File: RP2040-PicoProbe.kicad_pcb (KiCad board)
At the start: 4 copper layers, 39.4 x 17.8 mm, 47 parts, among them J1 CONN_MCU_DEBUG, J2 CONN_DBG_COMB, J5 USB_B_Micro, J7 CONN_DBG_JTAG, U1 W25Q128JVS, U2 RP2040, U3 74AUP1T17, U4 W25Q128JVEIQ, U5 MIC5205-3.3YM5, U6 74AUP1T17, Y1 12MHz

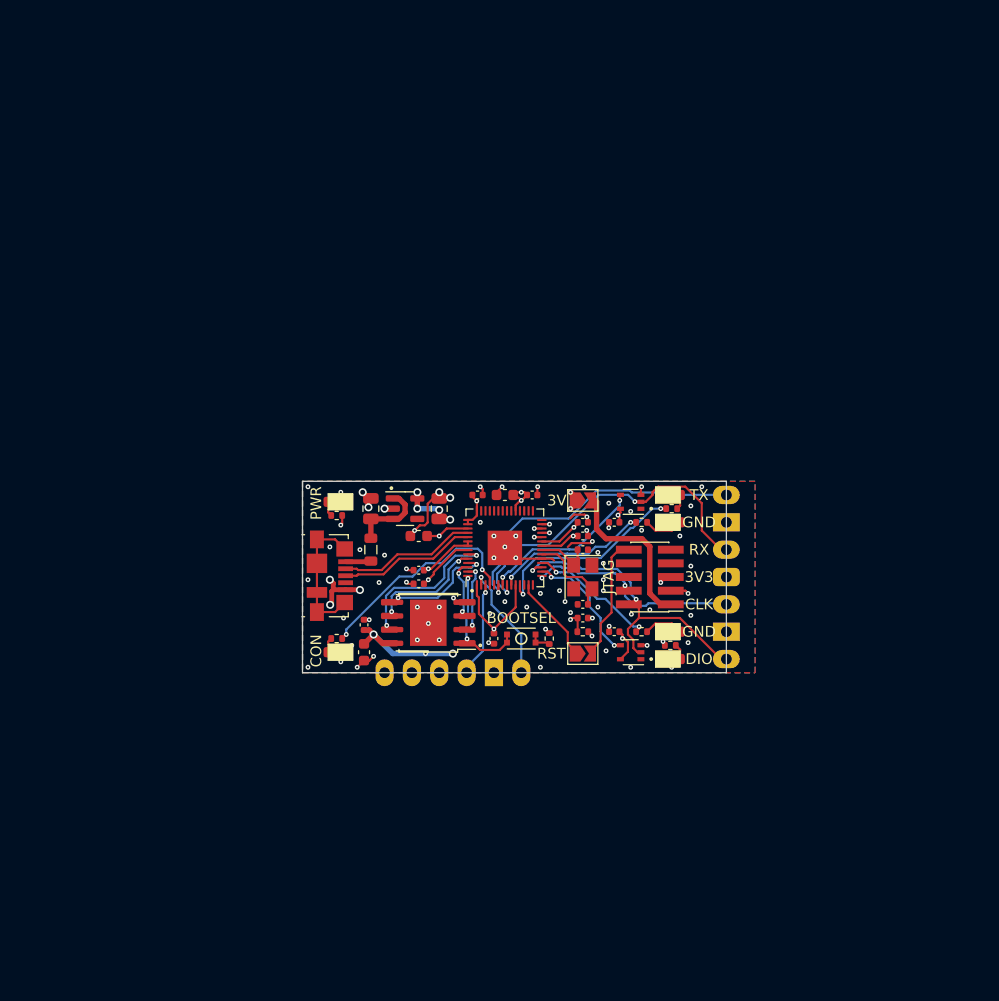
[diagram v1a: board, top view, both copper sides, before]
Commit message: Removed host debug part. Moved secondary components to the back of the board.
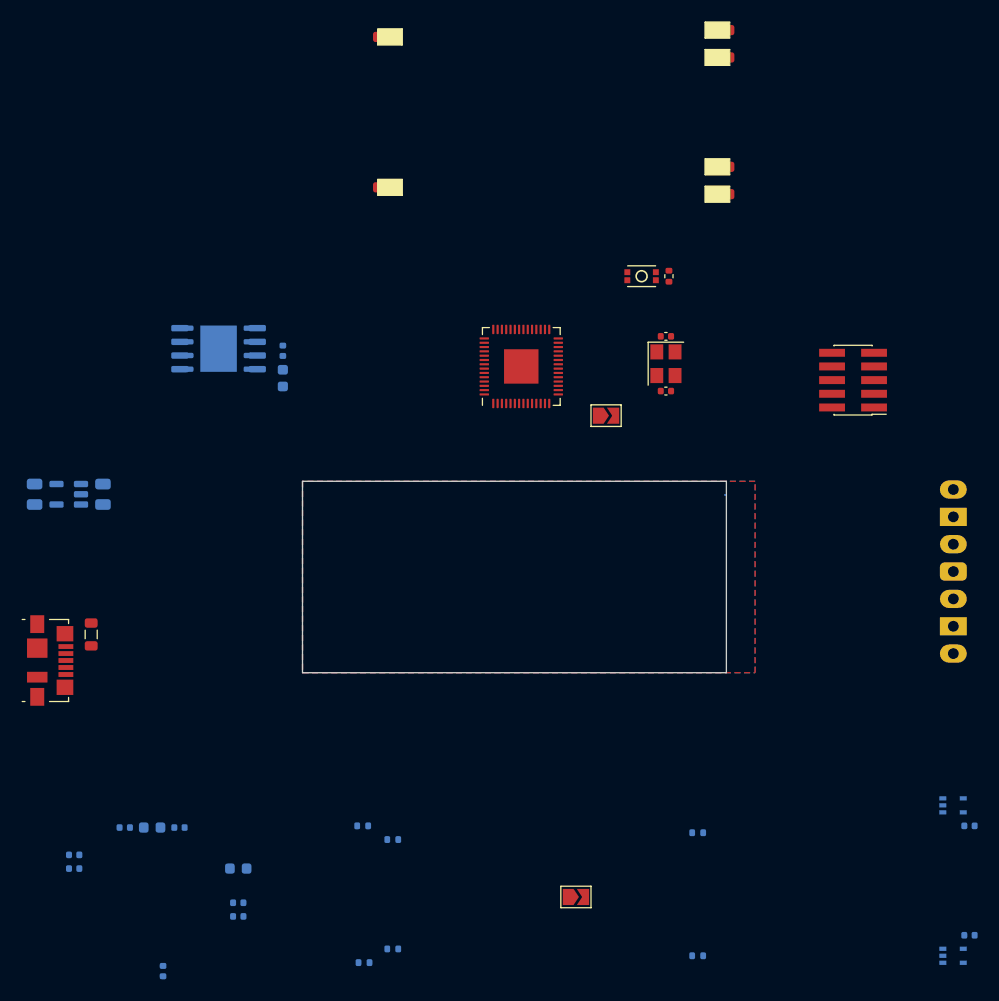
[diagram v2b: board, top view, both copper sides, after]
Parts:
- removed C12: 100nF, Capacitor_SMD:C_0402_1005Metric
- removed J1: CONN_MCU_DEBUG, Connector_PinHeader_2.54mm:PinHeader_1x06_P2.54mm_Vertical
- removed R8: 10k, Resistor_SMD:R_0402_1005Metric
- C1, C10, C11, C13, C14, C15, C16, C17, C18, C2, C4, C5, C6, C8, C9, R1, R2, R3, R4, R5, R6, U1, U3, U4, U5, U6: moved to B.Cu
- moved C11 56.4 mm to (105.8, 128.4), turned to 180 degrees
- moved C18 56.4 mm to (105.8, 127.2), turned to 180 degrees
- moved C4 48.9 mm to (110.5, 124.6), turned to 180 degrees
- moved C1 45.0 mm to (113.0, 124.6), turned to 0 degrees
- moved R3 44.6 mm to (163.7, 136.5), turned to 0 degrees
- moved R6 44.6 mm to (163.7, 125.1), turned to 0 degrees
- moved C10 43.6 mm to (114.0, 137.9)
- moved D1 43.4 mm to (165.9, 53.1)
- moved D2 43.4 mm to (134.8, 51.2)
- moved D5 43.4 mm to (134.8, 65.2)
- moved D4 43.4 mm to (165.9, 50.5)
- moved D6 43.4 mm to (165.9, 63.2)
- moved D7 43.4 mm to (165.9, 65.8)
- moved C13 43.4 mm to (188.9, 134.6), turned to 0 degrees
- moved C17 43.4 mm to (188.9, 124.5), turned to 0 degrees
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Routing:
- net +3V3: track 52.5 -> 0.00 mm, vias 19 -> 0
- net GND: track 43.4 -> 0.00 mm, vias 83 -> 0
- net TARGET_RX: track 32.4 -> 0.00 mm, vias 2 -> 0
- net +1V1: track 32.0 -> 0.00 mm, vias 3 -> 0
- net DBG_DIO: track 29.7 -> 0.00 mm, vias 2 -> 0
- net TARGET_TX: track 29.4 -> 0.02 mm, vias 1 -> 0
- net HOST_RESET: track 28.5 -> 0.00 mm, vias 2 -> 0
- net HOST_DIO: track 25.4 -> 0.00 mm, vias 1 -> 0
- net HOST_CLK: track 23.1 -> 0.00 mm, vias 1 -> 0
- net DBG_CLK: track 20.8 -> 0.00 mm, vias 2 -> 0
- net LED_ACT: track 20.1 -> 0.00 mm, vias 2 -> 0
- net LED_TX: track 18.8 -> 0.00 mm, vias 2 -> 0
- net LED_RUN: track 17.3 -> 0.00 mm, vias 2 -> 0
- net TARGET_3V3: track 15.5 -> 0.00 mm
- net UART_RX_BUF: track 15.4 -> 0.00 mm, vias 2 -> 0
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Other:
- board text removed: "${TITLE} ${COMPANY} ${COMMENT2}"
- board text removed: "3V"
- board text removed: "3V3"
- board text removed: "BOOTSEL"
- board text removed: "CLK"
- board text removed: "CON"
- board text removed: "DIO"
- board text removed: "GND"
- board text removed: "JTAG"
- board text removed: "PWR"
- board text removed: "RST"
- board text removed: "RX"
- board text removed: "TX"

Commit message: Roughly put components to their places
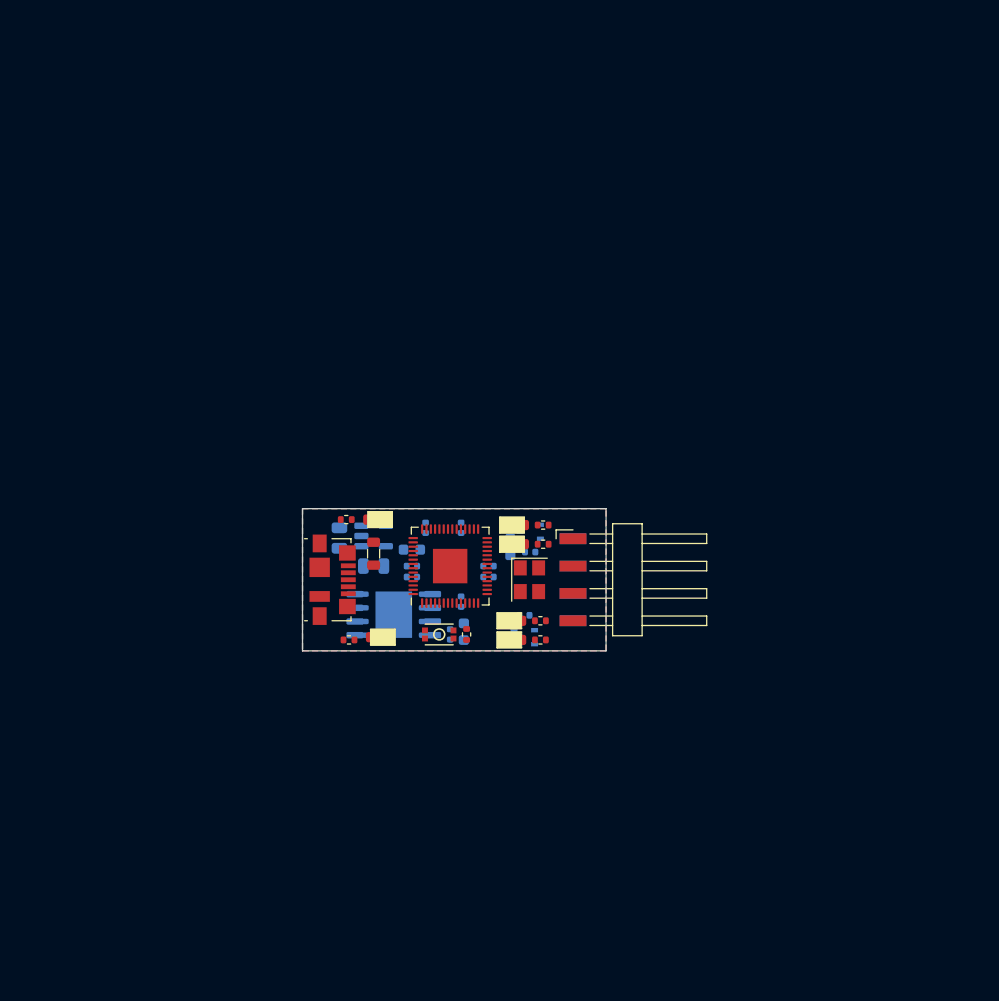
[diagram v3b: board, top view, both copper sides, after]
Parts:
- removed C19, C20: 12pF, Capacitor_SMD:C_0402_1005Metric
- removed J7: CONN_DBG_JTAG, Connector_PinHeader_1.27mm:PinHeader_2x05_P1.27mm_Vertical_SMD
- removed JP1: SJ_JTAG_3V3, Jumper:SolderJumper-2_P1.3mm_Open_TrianglePad1.0x1.5mm
- removed JP2: SJ_RESET, Jumper:SolderJumper-2_P1.3mm_Open_TrianglePad1.0x1.5mm
- added J1: CONN_UART, Connector_Harwin:Harwin_M20-89004xx_1x04_P2.54mm_Horizontal, F.Cu at (157.6, 101.6)
- J2: value CONN_DBG_COMB -> CONN_DBG; footprint Connector_PinSocket_2.54mm:PinSocket_1x07_P2.54mm_Vertical -> Connector_Harwin:Harwin_M20-89004xx_1x04_P2.54mm_Horizontal; moved to B.Cu
- R1, R2, R3, R4, R5, R6: moved to F.Cu
- moved D2 55.8 mm to (134.1, 106.9)
- moved U6 55.6 mm to (148.1, 97.1)
- moved C13 54.1 mm to (148.1, 99.0), turned to 180 degrees
- moved R3 52.0 mm to (131.1, 96.0)
- moved D4 49.8 mm to (146.8, 96.5)
- moved D1 49.1 mm to (146.8, 98.3)
- moved C11 47.1 mm to (144.3, 101.3)
- moved C18 46.9 mm to (144.3, 100.3)
- moved D6 46.4 mm to (146.6, 105.4)
- moved C17 45.7 mm to (147.6, 104.9), turned to 180 degrees
- moved D7 45.7 mm to (146.6, 107.2)
- moved C10 44.1 mm to (141.7, 103.6), turned to 90 degrees
- moved U3 42.8 mm to (147.6, 106.9)
- moved C1 42.3 mm to (146.3, 98.6), turned to 90 degrees
- moved C4 39.4 mm to (138.4, 96.8), turned to -90 degrees
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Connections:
- net HOST_CLK renamed MCU_CLK
- net HOST_DIO renamed MCU_DIO
- net HOST_RESET renamed MCU_RESET
- net HOST_RX renamed MCU_RX
- net HOST_TX renamed MCU_TX
- J2 pad 1: TARGET_TX -> DBG_CLK
- J2 pad 3: TARGET_RX -> DBG_DIO
- J2 pad 4: +3V3 -> VUSB
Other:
- board size 39.4 x 17.8 mm -> 28.2 x 13.2 mm

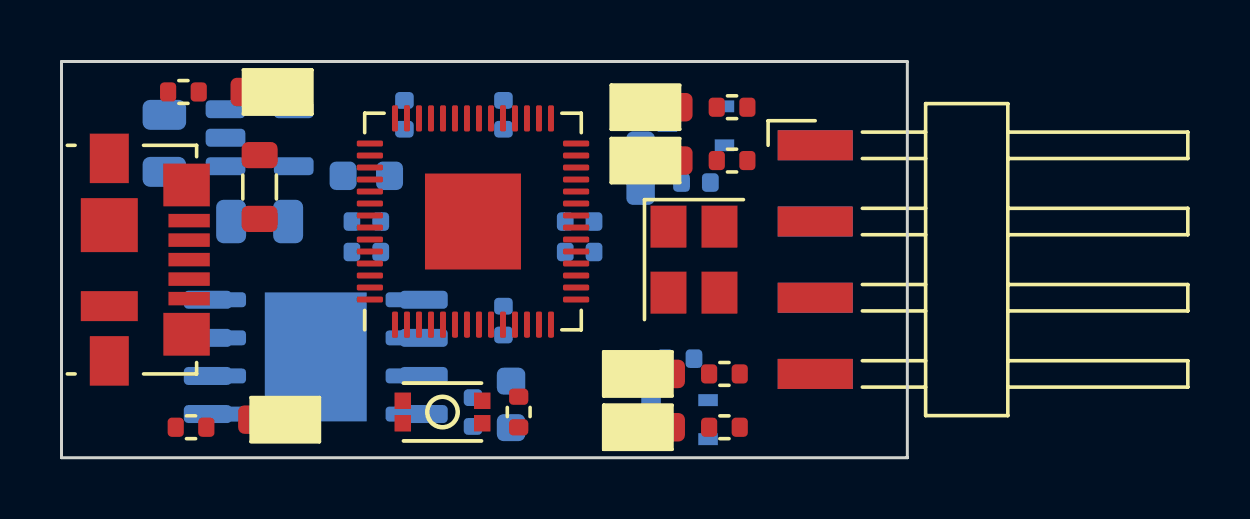
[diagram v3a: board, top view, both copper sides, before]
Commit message: Made the board smaller. Organized components to their expected locations.
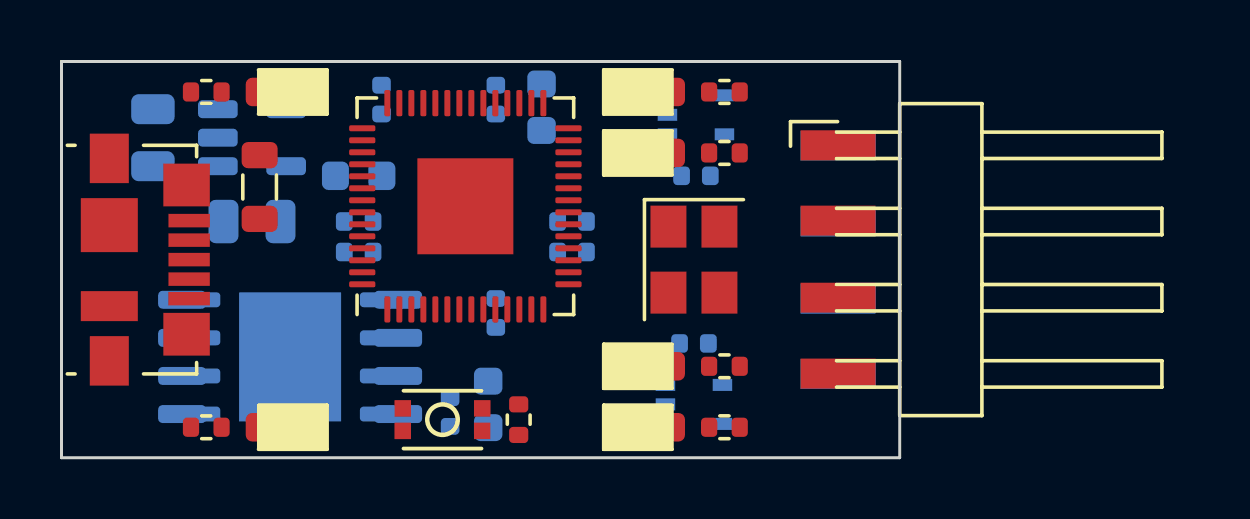
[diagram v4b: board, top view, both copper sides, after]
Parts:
- moved C1 3.88 mm to (143.0, 96.5), turned to -90 degrees
- moved J1 2.71 mm to (154.9, 101.6)
- moved J2 2.71 mm to (154.9, 101.6)
- moved C4 0.92 mm to (137.7, 96.3)
- moved U1 0.86 mm to (134.6, 104.8)
- moved U4 0.86 mm to (134.6, 104.8)
- moved C16 0.76 mm to (141.2, 106.4)
- moved C2 0.76 mm to (140.0, 106.7), turned to -90 degrees
- moved R3 0.76 mm to (131.8, 96.0)
- moved C17 0.70 mm to (148.1, 104.4)
- moved U3 0.70 mm to (148.1, 106.4)
- moved D4 0.57 mm to (146.6, 96.0)
- moved U2 0.57 mm to (140.5, 99.8)
- moved C6 0.57 mm to (141.5, 96.3)
- moved R2 0.57 mm to (149.1, 96.0)
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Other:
- board size 28.2 x 13.2 mm -> 27.9 x 13.2 mm

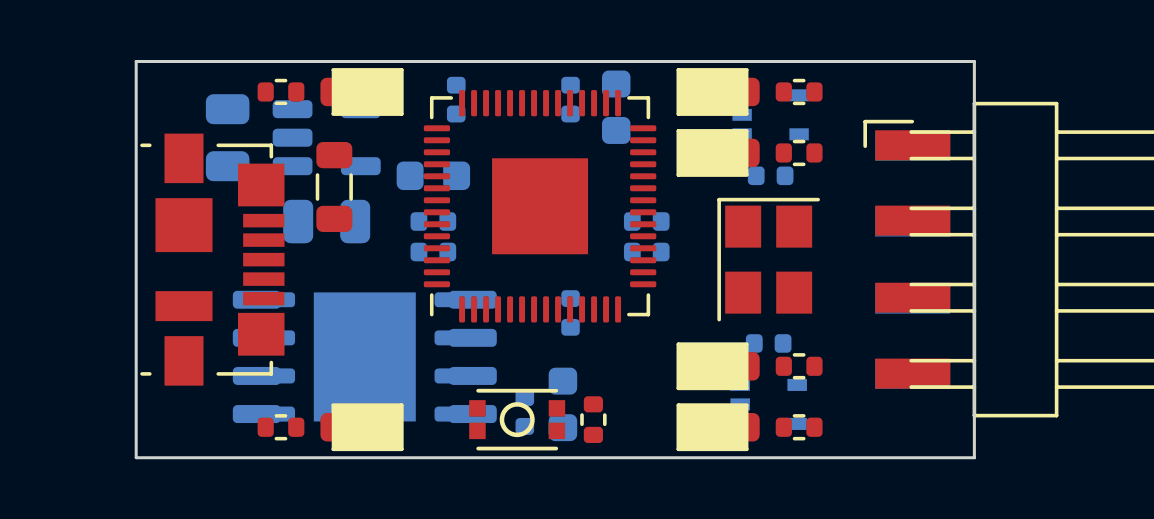
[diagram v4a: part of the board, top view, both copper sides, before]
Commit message: Added traces between components
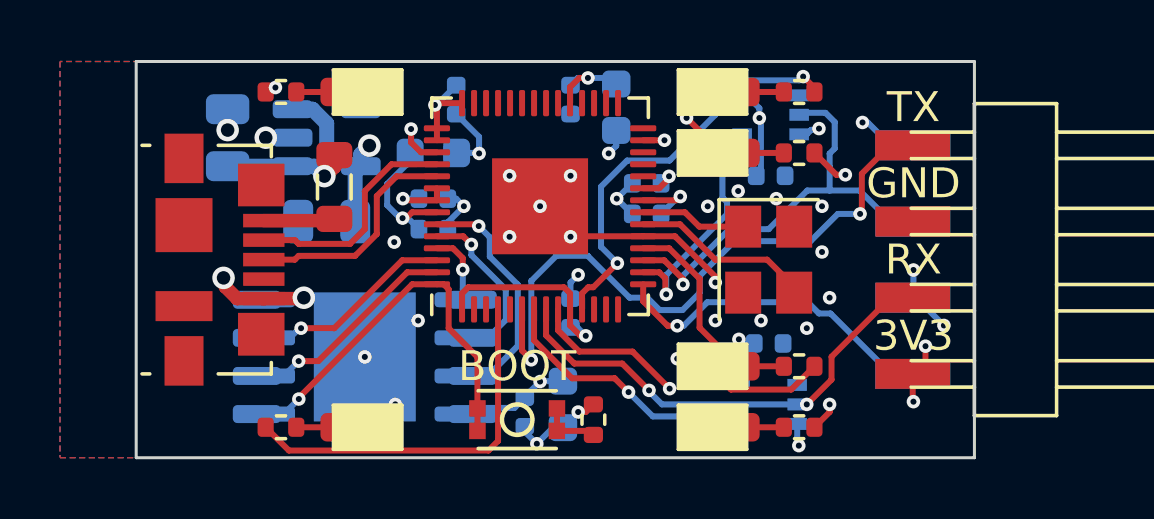
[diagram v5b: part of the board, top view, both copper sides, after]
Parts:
- moved D2 11.2 mm to (134.4, 96.0)
- moved D5 11.2 mm to (134.4, 107.2)
- moved R3 11.2 mm to (131.8, 107.2)
- moved R6 11.2 mm to (131.8, 96.0), turned to 0 degrees
- moved C11 1.27 mm to (144.0, 100.1)
- moved C18 1.27 mm to (144.0, 99.1)
- moved C5 0.76 mm to (136.9, 98.0)
- moved C8 0.76 mm to (136.9, 99.6)
- moved C9 0.76 mm to (136.9, 100.6)
- turned C13 to 0 degrees
- turned C17 to 0 degrees
- turned R1 to 180 degrees
- turned R2 to 180 degrees
- turned U3 to 180 degrees
- turned U6 to 180 degrees
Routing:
- net +3V3: track 0.00 -> 30.8 mm, vias 0 -> 12
- net VUSB: track 0.00 -> 29.2 mm, vias 0 -> 2
- net GND: track 0.00 -> 27.5 mm, vias 0 -> 39
- net TARGET_TX: track 0.00 -> 21.6 mm, vias 0 -> 2
- net LED_RX: track 0.00 -> 20.9 mm, vias 0 -> 2
- net +1V1: track 0.00 -> 17.8 mm, vias 0 -> 3
- net TARGET_RX: track 0.00 -> 16.0 mm, vias 0 -> 2
- net DBG_DIO: track 0.00 -> 15.0 mm, vias 0 -> 1
- net LED_TX: track 0.00 -> 14.3 mm, vias 0 -> 2
- net LED_RUN: track 0.00 -> 12.8 mm, vias 0 -> 2
- net LED_ACT: track 0.00 -> 12.6 mm
- net QSPI_SS: track 0.00 -> 12.5 mm, vias 0 -> 1
- net DBG_CLK: track 0.00 -> 11.2 mm, vias 0 -> 1
- net LED_CON: track 0.00 -> 9.53 mm
- net UART_RX_BUF: track 0.00 -> 9.06 mm, vias 0 -> 1
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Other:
- board text added: "3V3"
- board text added: "5V"
- board text added: "BOOT"
- board text added: "CLK"
- board text added: "DIO"
- board text added: "GND"
- board text added: "RX"
- board text added: "TX"
